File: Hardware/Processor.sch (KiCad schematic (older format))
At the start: 15 parts, among them J1 ICSP-PIC, J2 USB_MINI, SW1 PGM, SW2 RST, U5 PIC32MX250F128B, X1 8MHz

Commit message: Switch to 44 pin PIC
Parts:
- removed U5: PIC32MX250F128B, symbol PIC32MX250F128B
- added C41: 0.1uF, CAPC1608, symbol C
- added R31: 10k, RESC1608, symbol R
- added R32: 10, ~, symbol R
- added U5: PIC32MX250F128D, ~, symbol PIC32MX250F128D
- R15: value R -> 10k; footprint ~ -> RESC1608; Distributor Part No (none) -> RMCF0603JT10K0CT-ND; MFR Name (none) -> Stackpole; MFR Part No (none) -> RMCF0603JT10K0; Power W -> 0.1W; Tolerance % -> 5%
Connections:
- net labels added: VAng
- wire segments 63 -> 76
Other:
- note removed: "A"
- moved on the sheet: J1, R14, SW2

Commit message: Add external connector
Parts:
- added J3: CONN-9, ~, symbol CONN-9
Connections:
- net labels added: SCL/DI, SDA/DO, VCOM
- net labels removed: SCL, SDA
- wire segments 76 -> 84
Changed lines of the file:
@@
 Sheet 5 8
 Title "Solid State Cosmic Ray Detector"
-Date "20 dec 2013"
+Date "21 dec 2013"
 Rev "1"
 Comp "Ethan Harstad"
@@
 Text HLabel 9400 4000 2    60   Input ~ 0
 A2
-Text Label 5200 4800 2    60   ~ 0
-SCL
-Text Label 5200 4700 2    60   ~ 0
-SDA
 $Comp
 L C C20
@@
 Wire Wire Line
 	9100 4300 9400 4300
+Text Label 7400 2100 2    60   ~ 0
+SDA/DO
+Text Label 9400 3100 0    60   ~ 0
+SCL/DI
+Wire Wire Line
+	9400 3100 9100 3100
+Wire Wire Line
+	7400 2100 7700 2100
+$Comp
+L CONN-9 J3
+U 1 1 52B50B8D
+P 9800 6000
+F 0 "J3" H 9800 6500 60  0000 C CNN
+F 1 "CONN-9" H 9800 5500 60  0000 C CNN
+F 2 "~" H 9800 6050 60  0000 C CNN
+F 3 "~" H 9800 6050 60  0000 C CNN
+F 4 "TE" H 9800 6000 60  0001 C CNN "MFR Name"
+F 5 "1734354-1" H 9800 6000 60  0001 C CNN "MFR Part No"
+F 6 "A35107-ND" H 9800 6000 60  0001 C CNN "Distributor Part No"
+	1    9800 6000
+	-1   0    0    -1
+$EndComp
+$Comp
+L GND #PWR048
+U 1 1 52B50B9C
+P 9300 6500
+F 0 "#PWR048" H 9300 6500 30  0001 C CNN
+F 1 "GND" H 9300 6430 30  0001 C CNN
+F 2 "" H 9300 6500 60  0000 C CNN
+F 3 "" H 9300 6500 60  0000 C CNN
+	1    9300 6500
+	1    0    0    -1
+$EndComp
+Wire Wire Line
+	9300 6500 9300 6000
+Wire Wire Line
+	9300 6000 9400 6000
+$Comp
+L VCOM #PWR42
+U 1 1 52B50CC7
+P 9300 5500
+F 0 "#PWR42" H 9300 5700 40  0001 C CNN
+F 1 "VCOM" H 9300 5650 40  0000 C CNN
+F 2 "" H 9300 5500 60  0000 C CNN
+F 3 "" H 9300 5500 60  0000 C CNN
+	1    9300 5500
+	1    0    0    -1
+$EndComp
+Wire Wire Line
+	9300 5500 9300 5900
+Wire Wire Line
+	9300 5900 9400 5900
+Text Label 9200 5700 2    60   ~ 0
+SDA/DO
+Text Label 9200 5800 2    60   ~ 0
+SCL/DI
+Wire Wire Line
+	9200 5700 9400 5700
+Wire Wire Line
+	9200 5800 9400 5800
 $EndSCHEMATC

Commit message: Change to vertical USB port
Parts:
- J2: Distributor Part No ED2992CT-ND -> 732-2735-ND; MFR Name On Shore Technology -> Wurth; MFR Part No USB-M26FTR -> 651005136421
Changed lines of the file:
@@
 Sheet 5 8
 Title "Solid State Cosmic Ray Detector"
-Date "21 dec 2013"
+Date "22 dec 2013"
 Rev "1"
 Comp "Ethan Harstad"
@@
 F 2 "~" H 2100 3850 60  0000 C CNN
 F 3 "~" H 2100 3850 60  0000 C CNN
-F 4 "On Shore Technology" H 2100 3850 60  0001 C CNN "MFR Name"
-F 5 "USB-M26FTR" H 2100 3850 60  0001 C CNN "MFR Part No"
-F 6 "ED2992CT-ND" H 2100 3850 60  0001 C CNN "Distributor Part No"
+F 4 "Wurth" H 2100 3850 60  0001 C CNN "MFR Name"
+F 5 "651005136421" H 2100 3850 60  0001 C CNN "MFR Part No"
+F 6 "732-2735-ND" H 2100 3850 60  0001 C CNN "Distributor Part No"
 	1    2100 3850
 	-1   0    0    -1

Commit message: Add additional photodiodes
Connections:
- wire segments 84 -> 97
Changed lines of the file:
@@
 $EndComp
 $Comp
-L +3.3V #PWR031
+L +3.3V #PWR039
 U 1 1 5240FDA6
 P 2500 1000
-F 0 "#PWR031" H 2500 960 30  0001 C CNN
+F 0 "#PWR039" H 2500 960 30  0001 C CNN
 F 1 "+3.3V" H 2500 1110 30  0000 C CNN
 F 2 "" H 2500 1000 60  0000 C CNN
@@
 $EndComp
 $Comp
-L GND #PWR032
+L GND #PWR040
 U 1 1 5240FDF5
 P 2500 2300
-F 0 "#PWR032" H 2500 2300 30  0001 C CNN
+F 0 "#PWR040" H 2500 2300 30  0001 C CNN
 F 1 "GND" H 2500 2230 30  0001 C CNN
 F 2 "" H 2500 2300 60  0000 C CNN
@@
 OSC2
 $Comp
-L GND #PWR033
+L GND #PWR041
 U 1 1 5240FF54
 P 2100 5900
-F 0 "#PWR033" H 2100 5900 30  0001 C CNN
+F 0 "#PWR041" H 2100 5900 30  0001 C CNN
 F 1 "GND" H 2100 5830 30  0001 C CNN
 F 2 "" H 2100 5900 60  0000 C CNN
@@
 $EndComp
 $Comp
-L GND #PWR034
+L GND #PWR042
 U 1 1 5240FF63
 P 2800 5900
-F 0 "#PWR034" H 2800 5900 30  0001 C CNN
+F 0 "#PWR042" H 2800 5900 30  0001 C CNN
 F 1 "GND" H 2800 5830 30  0001 C CNN
 F 2 "" H 2800 5900 60  0000 C CNN
@@
 $EndComp
 $Comp
-L +3.3V #PWR035
+L +3.3V #PWR043
 U 1 1 5240FFFE
 P 9300 2000
-F 0 "#PWR035" H 9300 1960 30  0001 C CNN
+F 0 "#PWR043" H 9300 1960 30  0001 C CNN
 F 1 "+3.3V" H 9300 2110 30  0000 C CNN
 F 2 "" H 9300 2000 60  0000 C CNN
@@
 $EndComp
 $Comp
-L +3.3V #PWR036
+L +3.3V #PWR044
 U 1 1 524100A6
 P 7500 2000
-F 0 "#PWR036" H 7500 1960 30  0001 C CNN
+F 0 "#PWR044" H 7500 1960 30  0001 C CNN
 F 1 "+3.3V" H 7500 2110 30  0000 C CNN
 F 2 "" H 7500 2000 60  0000 C CNN
@@
 $EndComp
 $Comp
-L GND #PWR037
+L GND #PWR045
 U 1 1 5241010B
 P 2100 7200
-F 0 "#PWR037" H 2100 7200 30  0001 C CNN
+F 0 "#PWR045" H 2100 7200 30  0001 C CNN
 F 1 "GND" H 2100 7130 30  0001 C CNN
 F 2 "" H 2100 7200 60  0000 C CNN
@@
 VCap
 $Comp
-L GND #PWR038
+L GND #PWR046
 U 1 1 524101F5
 P 2500 4200
-F 0 "#PWR038" H 2500 4200 30  0001 C CNN
+F 0 "#PWR046" H 2500 4200 30  0001 C CNN
 F 1 "GND" H 2500 4130 30  0001 C CNN
 F 2 "" H 2500 4200 60  0000 C CNN
@@
 ID
 $Comp
-L +3.3V #PWR039
+L +3.3V #PWR047
 U 1 1 524102C8
 P 3000 6400
-F 0 "#PWR039" H 3000 6360 30  0001 C CNN
+F 0 "#PWR047" H 3000 6360 30  0001 C CNN
 F 1 "+3.3V" H 3000 6510 30  0000 C CNN
 F 2 "" H 3000 6400 60  0000 C CNN
@@
 $EndComp
 $Comp
-L GND #PWR040
+L GND #PWR048
 U 1 1 5241033E
 P 3000 7300
-F 0 "#PWR040" H 3000 7300 30  0001 C CNN
+F 0 "#PWR048" H 3000 7300 30  0001 C CNN
 F 1 "GND" H 3000 7230 30  0001 C CNN
 F 2 "" H 3000 7300 60  0000 C CNN
@@
 $EndComp
 $Comp
-L GND #PWR041
+L GND #PWR049
 U 1 1 5241051A
 P 5400 2000
-F 0 "#PWR041" H 5400 2000 30  0001 C CNN
+F 0 "#PWR049" H 5400 2000 30  0001 C CNN
 F 1 "GND" H 5400 1930 30  0001 C CNN
 F 2 "" H 5400 2000 60  0000 C CNN
@@
 $EndComp
 $Comp
-L +3.3V #PWR042
+L +3.3V #PWR050
 U 1 1 52410529
 P 6100 1200
-F 0 "#PWR042" H 6100 1160 30  0001 C CNN
+F 0 "#PWR050" H 6100 1160 30  0001 C CNN
 F 1 "+3.3V" H 6100 1310 30  0000 C CNN
 F 2 "" H 6100 1200 60  0000 C CNN
@@
 $EndComp
 $Comp
-L GND #PWR043
+L GND #PWR051
 U 1 1 52410620
 P 6100 2500
-F 0 "#PWR043" H 6100 2500 30  0001 C CNN
+F 0 "#PWR051" H 6100 2500 30  0001 C CNN
 F 1 "GND" H 6100 2430 30  0001 C CNN
 F 2 "" H 6100 2500 60  0000 C CNN
@@
 $EndComp
 Wire Wire Line
-	2500 1000 2500 1900
+	2500 1000 2500 1100
+Wire Wire Line
+	2500 1100 2500 1900
 Wire Wire Line
 	2500 1900 2400 1900
@@
 	2500 2000 2500 2300
 Wire Wire Line
-	2400 1800 2800 1800
+	2400 1800 2700 1800
+Wire Wire Line
+	2700 1800 2800 1800
 Wire Wire Line
 	2700 1700 2700 1800
@@
 	2400 2200 2800 2200
 Wire Wire Line
-	2800 5100 2800 5300
-Wire Wire Line
-	2100 5100 2100 5300
+	2800 5100 2800 5200
+Wire Wire Line
+	2800 5200 2800 5300
+Wire Wire Line
+	2100 5100 2100 5200
+Wire Wire Line
+	2100 5200 2100 5300
 Wire Wire Line
 	2200 5200 2100 5200
@@
 	2400 3900 2600 3900
 Wire Wire Line
-	2400 4000 2600 4000
+	2400 4000 2500 4000
+Wire Wire Line
+	2500 4000 2600 4000
 Wire Wire Line
 	2400 4100 2500 4100
@@
 	2700 6600 2700 6500
 Wire Wire Line
-	2700 6500 3300 6500
+	2700 6500 3000 6500
+Wire Wire Line
+	3000 6500 3300 6500
 Wire Wire Line
 	2700 7100 2700 7200
 Wire Wire Line
-	2700 7200 3300 7200
+	2700 7200 3000 7200
+Wire Wire Line
+	3000 7200 3300 7200
 Wire Wire Line
 	3000 7200 3000 7300
@@
 	4700 1300 4800 1300
 Wire Wire Line
-	5300 1300 5500 1300
+	5300 1300 5400 1300
+Wire Wire Line
+	5400 1300 5500 1300
 Wire Wire Line
 	6100 1200 6100 1300
@@
 $EndComp
 Wire Wire Line
-	9300 2000 9300 4400
+	9300 2000 9300 2700
+Wire Wire Line
+	9300 2700 9300 4400
 Wire Wire Line
 	9300 2700 9100 2700
@@
 Connection ~ 9300 2700
 $Comp
-L GND #PWR044
+L GND #PWR052
 U 1 1 52B36F90
 P 7600 5000
-F 0 "#PWR044" H 7600 5000 30  0001 C CNN
+F 0 "#PWR052" H 7600 5000 30  0001 C CNN
 F 1 "GND" H 7600 4930 30  0001 C CNN
 F 2 "" H 7600 5000 60  0000 C CNN
@@
 $EndComp
 $Comp
-L GND #PWR045
+L GND #PWR053
 U 1 1 52B36F9F
 P 9200 5000
-F 0 "#PWR045" H 9200 5000 30  0001 C CNN
+F 0 "#PWR053" H 9200 5000 30  0001 C CNN
 F 1 "GND" H 9200 4930 30  0001 C CNN
 F 2 "" H 9200 5000 60  0000 C CNN
@@
 $EndComp
 Wire Wire Line
-	9200 2600 9200 5000
+	9200 2600 9200 4500
+Wire Wire Line
+	9200 4500 9200 5000
 Wire Wire Line
 	9200 4500 9100 4500
@@
 	7700 2600 7600 2600
 Wire Wire Line
-	7600 2600 7600 5000
+	7600 2600 7600 4300
+Wire Wire Line
+	7600 4300 7600 5000
 Wire Wire Line
 	7700 4300 7600 4300
 Connection ~ 7600 4300
 Wire Wire Line
-	7500 3700 7500 4400
+	7500 3700 7500 3800
+Wire Wire Line
+	7500 3800 7500 4400
 Wire Wire Line
 	7500 4400 7700 4400
 Wire Wire Line
-	7500 2000 7500 3200
+	7500 2000 7500 3000
+Wire Wire Line
+	7500 3000 7500 3200
 Wire Wire Line
 	7400 2700 7700 2700
@@
 	7400 4900 7700 4900
 $Comp
-L +3.3V #PWR046
+L +3.3V #PWR054
 U 1 1 52B3737A
 P 2500 3000
-F 0 "#PWR046" H 2500 2960 30  0001 C CNN
+F 0 "#PWR054" H 2500 2960 30  0001 C CNN
 F 1 "+3.3V" H 2500 3110 30  0000 C CNN
 F 2 "" H 2500 3000 60  0000 C CNN
@@
 $EndComp
 $Comp
-L GND #PWR047
+L GND #PWR055
 U 1 1 52B37534
 P 3900 7200
-F 0 "#PWR047" H 3900 7200 30  0001 C CNN
+F 0 "#PWR055" H 3900 7200 30  0001 C CNN
 F 1 "GND" H 3900 7130 30  0001 C CNN
 F 2 "" H 3900 7200 60  0000 C CNN
@@
 $EndComp
 $Comp
-L GND #PWR048
+L GND #PWR056
 U 1 1 52B50B9C
 P 9300 6500
-F 0 "#PWR048" H 9300 6500 30  0001 C CNN
+F 0 "#PWR056" H 9300 6500 30  0001 C CNN
 F 1 "GND" H 9300 6430 30  0001 C CNN
 F 2 "" H 9300 6500 60  0000 C CNN
@@
 	9300 6000 9400 6000
 $Comp
-L VCOM #PWR42
+L VCOM #PWR50
 U 1 1 52B50CC7
 P 9300 5500
-F 0 "#PWR42" H 9300 5700 40  0001 C CNN
+F 0 "#PWR50" H 9300 5700 40  0001 C CNN
 F 1 "VCOM" H 9300 5650 40  0000 C CNN
 F 2 "" H 9300 5500 60  0000 C CNN

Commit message: Add status LEDs
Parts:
- added D34, D35: LED-DUAL, ~, symbol LED-DUAL
- added R33, R34, R35, R36: 150, RESC1608, symbol R
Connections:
- wire segments 97 -> 95
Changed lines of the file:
@@
 $EndComp
 Wire Wire Line
-	2500 1000 2500 1100
-Wire Wire Line
-	2500 1100 2500 1900
+	2500 1000 2500 1900
 Wire Wire Line
 	2500 1900 2400 1900
@@
 	2500 2000 2500 2300
 Wire Wire Line
-	2400 1800 2700 1800
-Wire Wire Line
-	2700 1800 2800 1800
+	2400 1800 2800 1800
 Wire Wire Line
 	2700 1700 2700 1800
@@
 	2400 2200 2800 2200
 Wire Wire Line
-	2800 5100 2800 5200
-Wire Wire Line
-	2800 5200 2800 5300
-Wire Wire Line
-	2100 5100 2100 5200
-Wire Wire Line
-	2100 5200 2100 5300
+	2800 5100 2800 5300
+Wire Wire Line
+	2100 5100 2100 5300
 Wire Wire Line
 	2200 5200 2100 5200
@@
 	2400 3900 2600 3900
 Wire Wire Line
-	2400 4000 2500 4000
-Wire Wire Line
-	2500 4000 2600 4000
+	2400 4000 2600 4000
 Wire Wire Line
 	2400 4100 2500 4100
@@
 	2700 6600 2700 6500
 Wire Wire Line
-	2700 6500 3000 6500
-Wire Wire Line
-	3000 6500 3300 6500
+	2700 6500 3300 6500
 Wire Wire Line
 	2700 7100 2700 7200
 Wire Wire Line
-	2700 7200 3000 7200
-Wire Wire Line
-	3000 7200 3300 7200
+	2700 7200 3300 7200
 Wire Wire Line
 	3000 7200 3000 7300
@@
 	4700 1300 4800 1300
 Wire Wire Line
-	5300 1300 5400 1300
-Wire Wire Line
-	5400 1300 5500 1300
+	5300 1300 5500 1300
 Wire Wire Line
 	6100 1200 6100 1300
@@
 $EndComp
 Wire Wire Line
-	9300 2000 9300 2700
-Wire Wire Line
-	9300 2700 9300 4400
+	9300 2000 9300 4400
 Wire Wire Line
 	9300 2700 9100 2700
@@
 $EndComp
 Wire Wire Line
-	9200 2600 9200 4500
-Wire Wire Line
-	9200 4500 9200 5000
+	9200 2600 9200 5000
 Wire Wire Line
 	9200 4500 9100 4500
@@
 	7700 2600 7600 2600
 Wire Wire Line
-	7600 2600 7600 4300
-Wire Wire Line
-	7600 4300 7600 5000
+	7600 2600 7600 5000
 Wire Wire Line
 	7700 4300 7600 4300
 Connection ~ 7600 4300
 Wire Wire Line
-	7500 3700 7500 3800
-Wire Wire Line
-	7500 3800 7500 4400
+	7500 3700 7500 4400
 Wire Wire Line
 	7500 4400 7700 4400
 Wire Wire Line
-	7500 2000 7500 3000
-Wire Wire Line
-	7500 3000 7500 3200
+	7500 2000 7500 3200
 Wire Wire Line
 	7400 2700 7700 2700
@@
 	9300 6000 9400 6000
 $Comp
-L VCOM #PWR50
+L VCOM #PWR52
 U 1 1 52B50CC7
 P 9300 5500
-F 0 "#PWR50" H 9300 5700 40  0001 C CNN
+F 0 "#PWR52" H 9300 5700 40  0001 C CNN
 F 1 "VCOM" H 9300 5650 40  0000 C CNN
 F 2 "" H 9300 5500 60  0000 C CNN
@@
 Wire Wire Line
 	9200 5800 9400 5800
+$Comp
+L LED-DUAL D34
+U 1 1 52B697DA
+P 5350 3700
+F 0 "D34" H 5350 3950 60  0000 C CNN
+F 1 "LED-DUAL" H 5350 3450 60  0000 C CNN
+F 2 "~" H 5350 3800 60  0000 C CNN
+F 3 "~" H 5350 3800 60  0000 C CNN
+F 4 "Dialight" H 5350 3700 60  0001 C CNN "MFR Name"
+F 5 "553-0121F" H 5350 3700 60  0001 C CNN "MFR Part No"
+F 6 "350-1822-ND" H 5350 3700 60  0001 C CNN "Distributor Part No"
+F 7 "V" H 5750 4225 60  0001 C CNN "Voltage"
+F 8 "I" H 5850 4325 60  0001 C CNN "Current"
+	1    5350 3700
+	1    0    0    -1
+$EndComp
+$Comp
+L LED-DUAL D35
+U 1 1 52B69811
+P 5350 4400
+F 0 "D35" H 5350 4650 60  0000 C CNN
+F 1 "LED-DUAL" H 5350 4150 60  0000 C CNN
+F 2 "~" H 5350 4500 60  0000 C CNN
+F 3 "~" H 5350 4500 60  0000 C CNN
+F 4 "Dialight" H 5350 4400 60  0001 C CNN "MFR Name"
+F 5 "553-0122F" H 5350 4400 60  0001 C CNN "MFR Part No"
+F 6 "350-1825-ND" H 5350 4400 60  0001 C CNN "Distributor Part No"
+F 7 "V" H 5750 4925 60  0001 C CNN "Voltage"
+F 8 "I" H 5850 5025 60  0001 C CNN "Current"
+	1    5350 4400
+	1    0    0    -1
+$EndComp
+$Comp
+L R R33
+U 1 1 52B69862
+P 4750 3600
+F 0 "R33" H 4750 3700 50  0000 C CNN
+F 1 "150" H 4750 3600 50  0000 C CNN
+F 2 "RESC1608" H 4750 3600 60  0001 C CNN
+F 3 "~" H 4750 3600 60  0000 C CNN
+F 4 "Stackpole" H 4750 3600 60  0001 C CNN "MFR Name"
+F 5 "RMCF0603FT150R" H 4750 3600 60  0001 C CNN "MFR Part No"
+F 6 "RMCF0603FT150RCT-ND" H 4750 3600 60  0001 C CNN "Distributor Part No"
+F 7 "0.1W" H 4750 3500 50  0001 C CNN "Power"
+F 8 "%" H 4750 3400 50  0001 C CNN "Tolerance"
+	1    4750 3600
+	1    0    0    -1
+$EndComp
+$Comp
+L R R34
+U 1 1 52B6999E
+P 4750 3800
+F 0 "R34" H 4750 3900 50  0000 C CNN
+F 1 "150" H 4750 3800 50  0000 C CNN
+F 2 "RESC1608" H 4750 3800 60  0001 C CNN
+F 3 "~" H 4750 3800 60  0000 C CNN
+F 4 "Stackpole" H 4750 3800 60  0001 C CNN "MFR Name"
+F 5 "RMCF0603FT150R" H 4750 3800 60  0001 C CNN "MFR Part No"
+F 6 "RMCF0603FT150RCT-ND" H 4750 3800 60  0001 C CNN "Distributor Part No"
+F 7 "0.1W" H 4750 3700 50  0001 C CNN "Power"
+F 8 "%" H 4750 3600 50  0001 C CNN "Tolerance"
+	1    4750 3800
+	1    0    0    1
+$EndComp
+$Comp
+L R R35
+U 1 1 52B699A9
+P 4750 4300
+F 0 "R35" H 4750 4400 50  0000 C CNN
+F 1 "150" H 4750 4300 50  0000 C CNN
+F 2 "RESC1608" H 4750 4300 60  0001 C CNN
+F 3 "~" H 4750 4300 60  0000 C CNN
+F 4 "Stackpole" H 4750 4300 60  0001 C CNN "MFR Name"
+F 5 "RMCF0603FT150R" H 4750 4300 60  0001 C CNN "MFR Part No"
+F 6 "RMCF0603FT150RCT-ND" H 4750 4300 60  0001 C CNN "Distributor Part No"
+F 7 "0.1W" H 4750 4200 50  0001 C CNN "Power"
+F 8 "%" H 4750 4100 50  0001 C CNN "Tolerance"
+	1    4750 4300
+	1    0    0    -1
+$EndComp
+$Comp
+L R R36
+U 1 1 52B699B4
+P 4750 4500
+F 0 "R36" H 4750 4600 50  0000 C CNN
+F 1 "150" H 4750 4500 50  0000 C CNN
+F 2 "RESC1608" H 4750 4500 60  0001 C CNN
+F 3 "~" H 4750 4500 60  0000 C CNN
+F 4 "Stackpole" H 4750 4500 60  0001 C CNN "MFR Name"
+F 5 "RMCF0603FT150R" H 4750 4500 60  0001 C CNN "MFR Part No"
+F 6 "RMCF0603FT150RCT-ND" H 4750 4500 60  0001 C CNN "Distributor Part No"
+F 7 "0.1W" H 4750 4400 50  0001 C CNN "Power"
+F 8 "%" H 4750 4300 50  0001 C CNN "Tolerance"
+	1    4750 4500
+	1    0    0    1
+$EndComp
+$Comp
+L GND #PWR057
+U 1 1 52B699BC
+P 5700 3900
+F 0 "#PWR057" H 5700 3900 30  0001 C CNN
+F 1 "GND" H 5700 3830 30  0001 C CNN
+F 2 "" H 5700 3900 60  0000 C CNN
+F 3 "" H 5700 3900 60  0000 C CNN
+	1    5700 3900
+	1    0    0    -1
+$EndComp
+Wire Wire Line
+	5700 3900 5700 3800
+Wire Wire Line
+	5700 3800 5600 3800
+$Comp
+L +3.3V #PWR058
+U 1 1 52B69A3A
+P 4400 3500
+F 0 "#PWR058" H 4400 3460 30  0001 C CNN
+F 1 "+3.3V" H 4400 3610 30  0000 C CNN
+F 2 "" H 4400 3500 60  0000 C CNN
+F 3 "" H 4400 3500 60  0000 C CNN
+	1    4400 3500
+	1    0    0    -1
+$EndComp
+Wire Wire Line
+	4400 3500 4400 4500
+Wire Wire Line
+	4400 4500 4500 4500
+Wire Wire Line
+	4500 4300 4400 4300
+Connection ~ 4400 4300
+Wire Wire Line
+	4500 3800 4400 3800
+Connection ~ 4400 3800
+Wire Wire Line
+	4500 3600 4400 3600
+Connection ~ 4400 3600
+Wire Wire Line
+	5000 3600 5100 3600
+Wire Wire Line
+	5100 3800 5000 3800
+Wire Wire Line
+	5000 4300 5100 4300
+Wire Wire Line
+	5000 4500 5100 4500
 $EndSCHEMATC

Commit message: Connect LEDs
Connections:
- net labels added: Count1, Count2, CountC, LED0, LED1, LED2, PS
- wire segments 95 -> 109

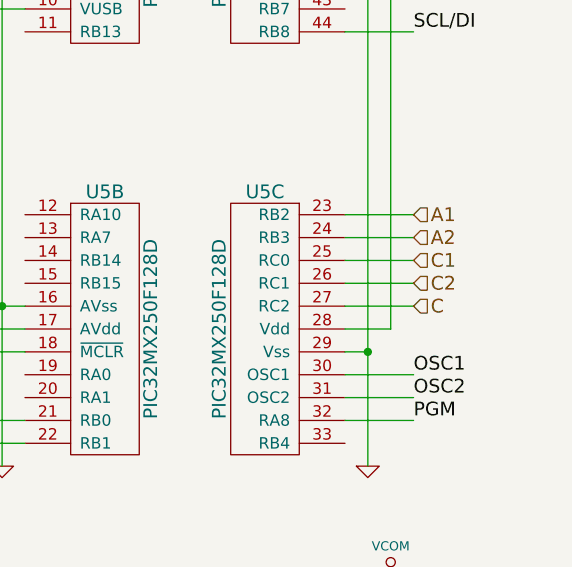
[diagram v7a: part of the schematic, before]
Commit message: Remove coincidence circuitry
PIC32 internal comparator has sufficient performance
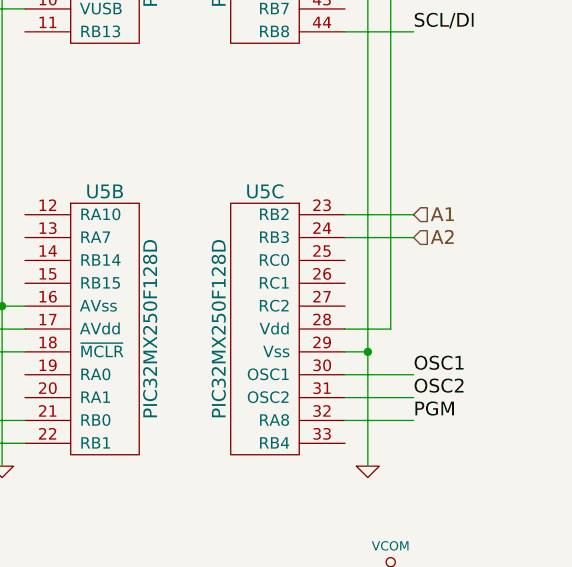
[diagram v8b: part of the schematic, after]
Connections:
- net labels removed: C, C1, C2
- wire segments 109 -> 106
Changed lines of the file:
@@
 $Descr A4 11693 8268
 encoding utf-8
-Sheet 5 8
+Sheet 4 7
 Title "Solid State Cosmic Ray Detector"
-Date "22 dec 2013"
+Date "24 dec 2013"
 Rev "1"
 Comp "Ethan Harstad"
@@
 Text Label 7400 2800 2    60   ~ 0
 D+
-Text HLabel 9400 4300 2    60   Input ~ 0
-C
-Text HLabel 9400 4100 2    60   Input ~ 0
-C1
-Text HLabel 9400 4200 2    60   Input ~ 0
-C2
 Text HLabel 9400 3900 2    60   Input ~ 0
 A1
@@
 	9100 4000 9400 4000
 Wire Wire Line
-	9100 4100 9400 4100
-Wire Wire Line
-	9100 4200 9400 4200
-Wire Wire Line
-	9100 4300 9400 4300
-Wire Wire Line
 	9400 3100 9100 3100
